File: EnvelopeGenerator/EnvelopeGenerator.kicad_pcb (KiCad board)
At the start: 2 copper layers, 49.5 x 97.8 mm, 49 parts, among them J1 Conn_01x02_Male, J2 Conn_01x03_Male, J3 Conn_01x09_Male, U1 L7812, U2 L7912, U3 AS3310, U4 LM741, U5 AS3360

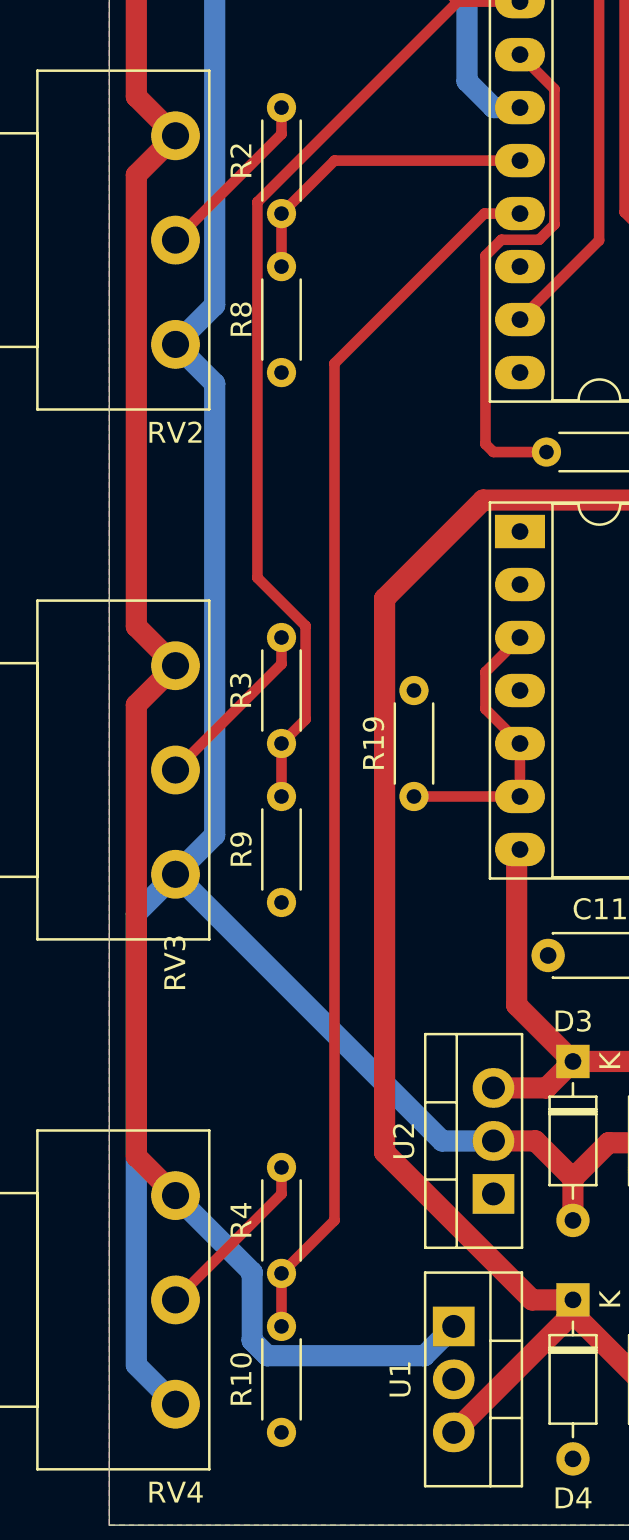
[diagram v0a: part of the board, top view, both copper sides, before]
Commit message: Designed and routed Envelope Filter PCB Also: * Finished Envelope Filter schematic * Exported cool RTX board render * Exported PDF of schematic * Began work on README
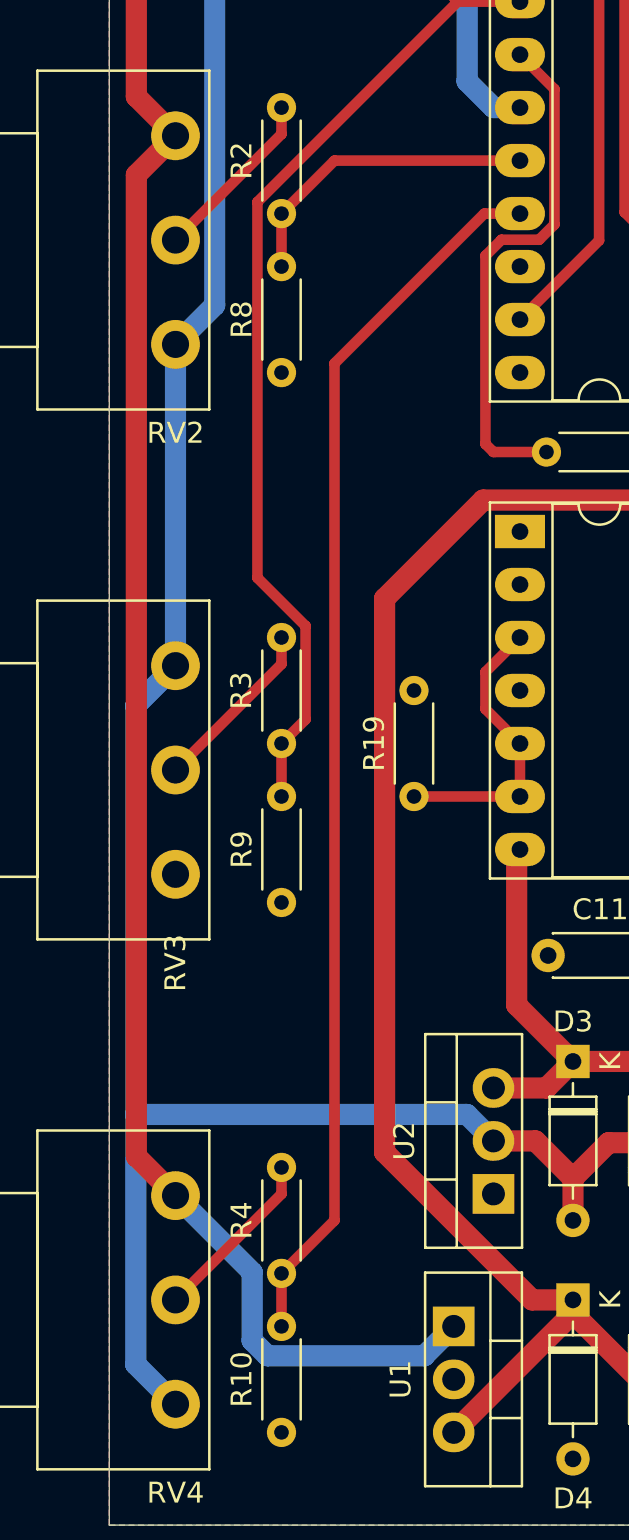
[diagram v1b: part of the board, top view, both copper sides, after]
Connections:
- RV3 pad 1: +15V -> -15V
- RV3 pad 3: -15V -> GND
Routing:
- net -15V: track 195.2 -> 190.8 mm
- net +15V: track 268.3 -> 266.7 mm
